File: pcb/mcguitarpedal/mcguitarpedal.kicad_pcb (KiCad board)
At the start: 2 copper layers, 123 x 113.5 mm, 123 parts, among them J1 OUT, J10 ENC2, J11 ENC3, J12 BTN_MTX, J2 EXP, J3 IN, J4 PWR, J5 PWR_IN, J6 PREAMP_HEADERS, J7 ILI9488 Module, J8 POT_HP_VOLUME_10k, J9 ENC1, Q1 2N3904, Q2 BC416, SW1 SW_PWR, SW2 SW_BYPASS, SW3 SW_TUNER, SW4 SW_PRESET, SW5 LINE_LEVEL, U1 Teensy4.1, U2 Teensy Audio Board, U3 LM4562, U4 STPDWN-3P-5V, U5 AMS1117-3.3, U6 74HCT595, U7 74HC148

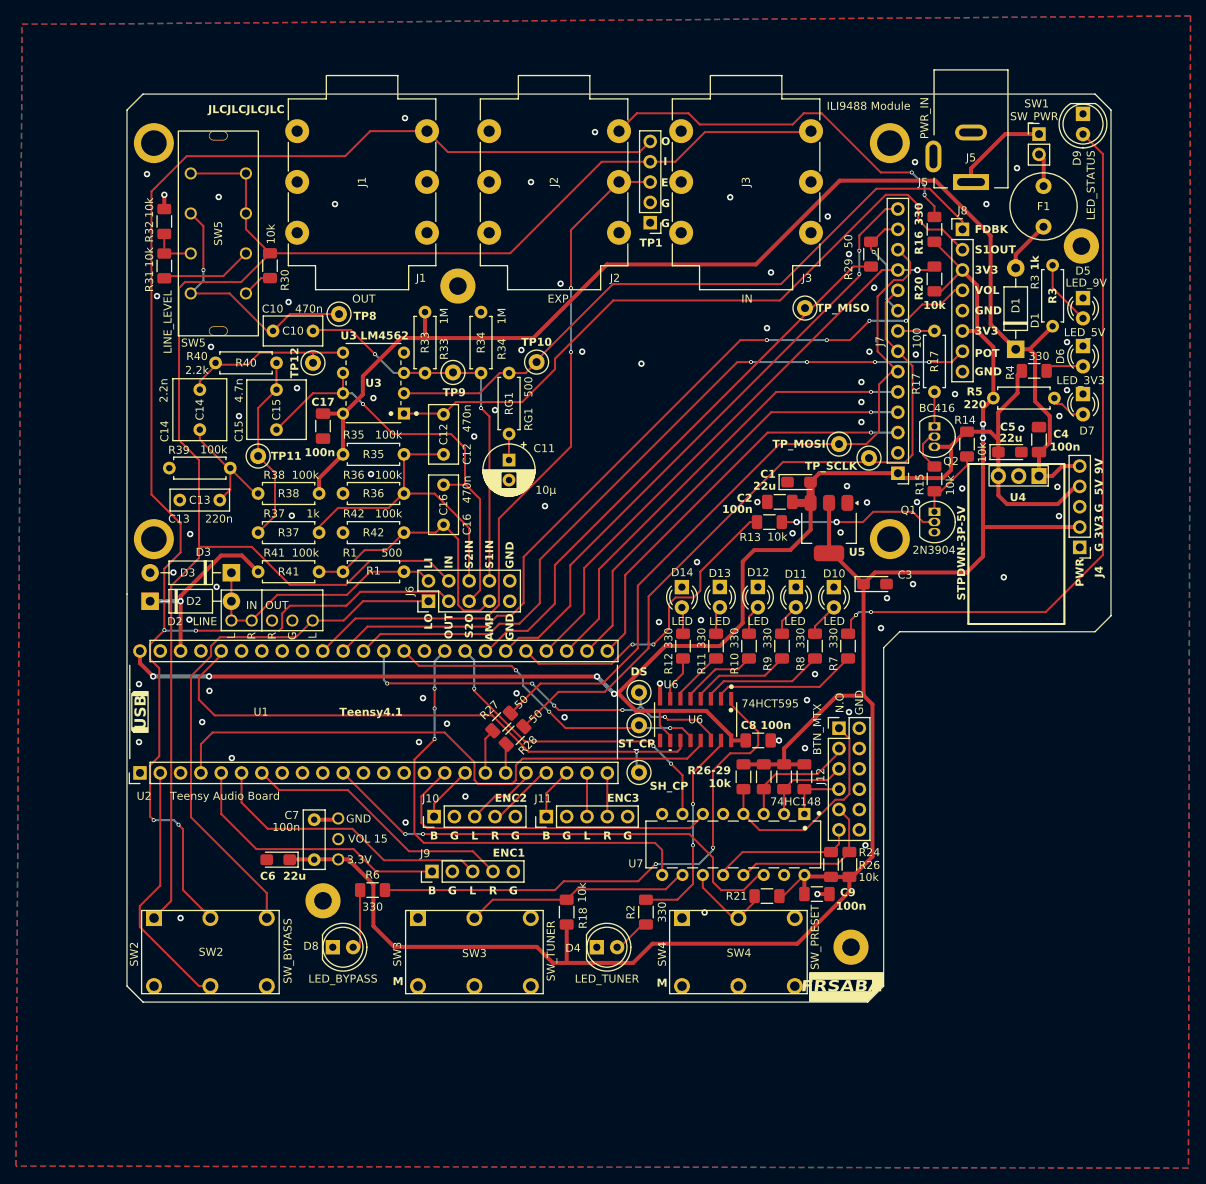
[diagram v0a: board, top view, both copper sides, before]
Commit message: Missing models, PCB pdf exports
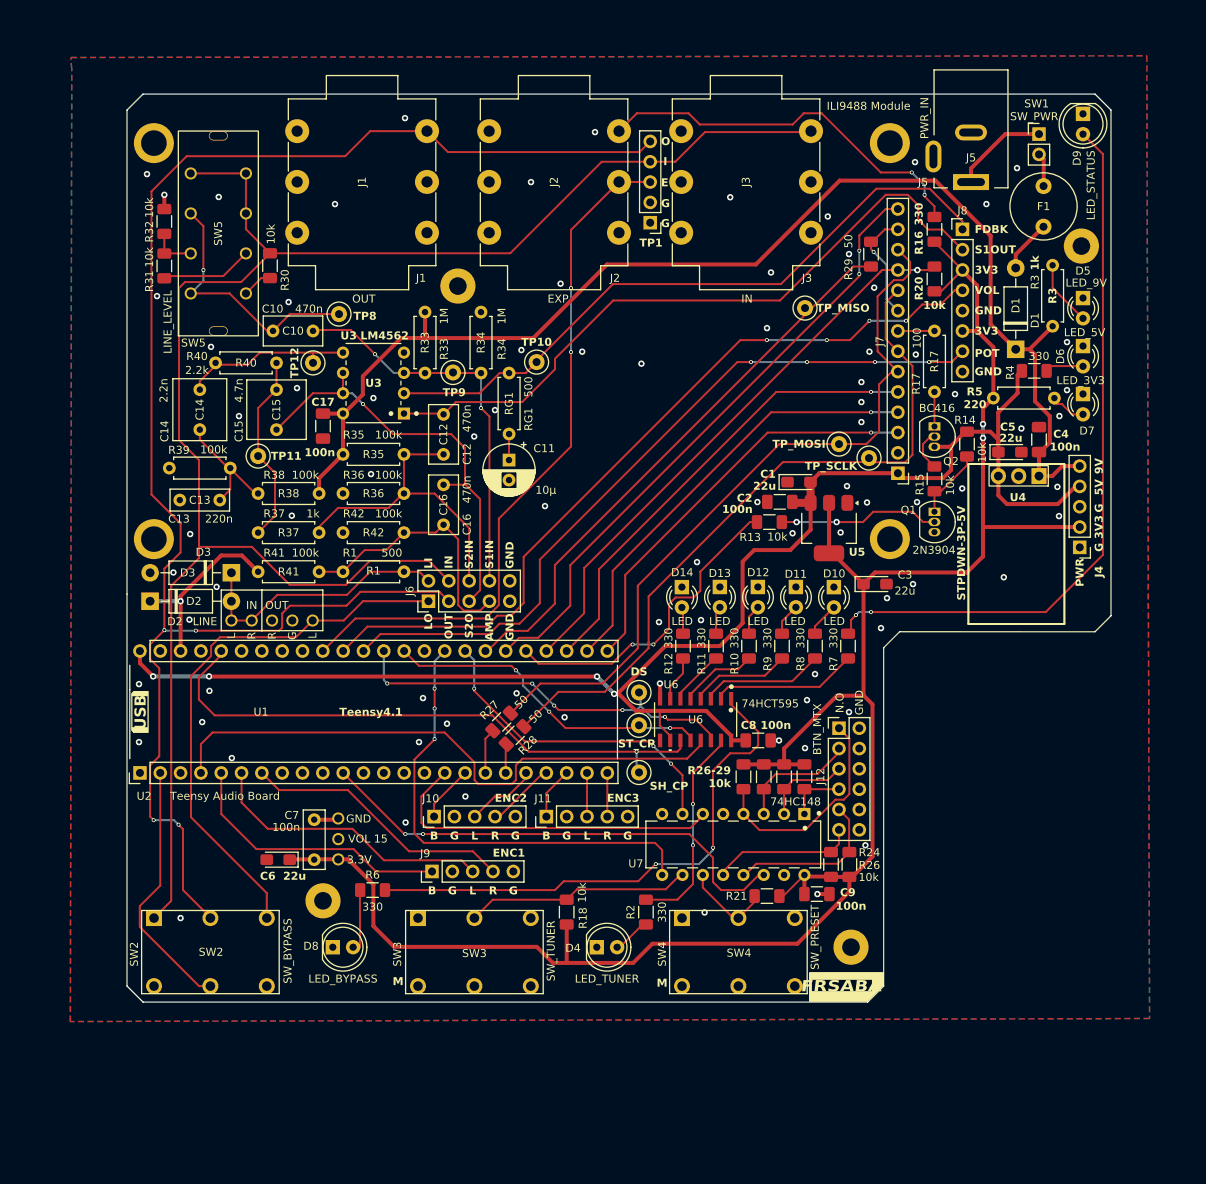
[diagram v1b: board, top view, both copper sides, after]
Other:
- board text removed: "JLCJLCJLCJLC"
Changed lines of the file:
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@@
 	)
 	(property "R_BIAS" "100k")
-	(property "R_BIAS_IN" "1M")
+	(property "R_BIAS_IN" "100k")
 	(net 0 "")
 	(net 1 "Net-(SW5-D)")
@@
 		)
 		(fp_text user "${REFERENCE}"
-			(at 0 0 360)
+			(at 0 0 0)
 			(layer "F.Fab")
 			(effects
@@
 		(property "Value" "22u"
 			(at 3.75 0.85 0)
-			(layer "F.Fab")
+			(layer "F.SilkS")
 			(effects
 				(font
@@
 			(pintype "power_in")
 		)
+		(model "${KICAD_MCGUITARPEDAL_MODELS}/P0008A.stp"
+			(offset
+				(xyz 3.78 -3.8 0)
+			)
+			(scale
+				(xyz 1 1 1)
+			)
+			(rotate
+				(xyz 0 0 0)
+			)
+		)
 	)
 	(footprint "mcguitarpedal:SW_PUSH_DPDT"
@@
 			(pintype "passive+no_connect")
 		)
-		(model "${KICAD8_3DMODEL_DIR}/Connector_BarrelJack.3dshapes/BarrelJack_Kycon_KLDX-0202-xC_Horizontal.wrl"
+		(model "${KIPRJMOD}/lib/3D_models/DC_Power_Jack_PCB_Mounted_2.1mm.step"
 			(offset
 				(xyz 0 0 0)
@@
 		(tags "resistor handsolder")
 		(property "Reference" "R16"
-			(at 1.691201 1.932 270)
+			(at 1.691201 1.932 -90)
 			(layer "F.SilkS")
 			(effects
@@
 		)
 		(property "Value" "330"
-			(at -1.908799 1.932 270)
+			(at -1.908799 1.932 -90)
 			(layer "F.SilkS")
 			(effects
@@
 			(pintype "power_in")
 		)
+		(model "${KIPRJMOD}/lib/74HCT595/SOIC-16_ONS.step"
+			(offset
+				(xyz 0 0 0)
+			)
+			(scale
+				(xyz 1 1 1)
+			)
+			(rotate
+				(xyz 0 0 0)
+			)
+		)
 	)
 	(footprint "mcguitarpedal:LED_D3.0mm"
@@
 		(tags "74HC148 ")
 		(property "Reference" "U7"
-			(at 6.211 21.076 180)
+			(at 6.211 21.076 360)
 			(layer "F.SilkS")
 			(effects
@@
 			(pintype "power_in")
 		)
+		(model "${KICAD_MCGUITARPEDAL_MODELS}/N16_TEX.step"
+			(offset
+				(xyz 0 0 0)
+			)
+			(scale
+				(xyz 1 1 1)
+			)
+			(rotate
+				(xyz 0 0 0)
+			)
+		)
 	)
 	(footprint "mcguitarpedal:Floating Encoder"
@@
 		)
 	)
-	(gr_text "JLCJLCJLCJLC"
-		(at 73.2 27.5 0)
-		(layer "F.SilkS")
-		(effects
-			(font
-				(size 1 1)
-				(thickness 0.2)
-				(bold yes)
-			)
-			(justify right bottom)
-		)
-	)
 	(gr_text "N.O"
 		(at 142.6 101.1 90)
@@
 	)
 	(zone
-		(net 43)
-		(net_name "Net-(J7-SCK)")
+		(net 42)
+		(net_name "Net-(J7-SDI(MOSI))")
 		(layer "F.Cu")
 		(name "$teardrop_padvia$")
 		(hatch full 0.1)
-		(priority 30002)
+		(priority 30001)
 		(attr
 			(teardrop
@@
 		(polygon
 			(pts
-				(xy 144.004509 71.125) (xy 144.278528 71.117413) (xy 144.530743 71.099433) (xy 144.759995 71.078226)
-				(xy 144.965124 71.06096) (xy 145.144971 71.054803) (xy 145.298374 71.066922) (xy 145.424175 71.104486)
-				(xy 145.521214 71.174662) (xy 146.251 70.5) (xy 145.31024 70.197149) (xy 145.256893 70.311335) (xy 145.169383 70.42805)
-				(xy 145.049097 70.541819) (xy 144.897419 70.647173) (xy 144.715736 70.73864) (xy 144.505433 70.810748)
-				(xy 144.267895 70.858025) (xy 144.004509 70.875)
+				(xy 144.9 68.625) (xy 144.610673 68.620769) (xy 144.343891 68.607147) (xy 144.101954 68.582738)
+				(xy 143.887163 68.546144) (xy 143.70182 68.49597) (xy 143.548227 68.430818) (xy 143.428683 68.349294)
+				(xy 143.345491 68.25) (xy 142.499 68.75) (xy 143.345491 69.25) (xy 143.428683 69.150705) (xy 143.548227 69.06918)
+				(xy 143.70182 69.004029) (xy 143.887163 68.953855) (xy 144.101954 68.917261) (xy 144.343891 68.892851)
+				(xy 144.610673 68.87923) (xy 144.9 68.875)
 			)
 		)
@@
 		(name "$teardrop_padvia$")
 		(hatch full 0.1)
-		(priority 30005)
+		(priority 30004)
 		(attr
 			(teardrop
@@
 		(polygon
 			(pts
-				(xy 140.127604 50.55122) (xy 139.933634 50.717404) (xy 139.734444 50.839839) (xy 139.535594 50.922862)
-				(xy 139.342646 50.970808) (xy 139.161163 50.988016) (xy 138.996706 50.978821) (xy 138.854835 50.947561)
-				(xy 138.741115 50.898572) (xy 138.249293 51.750707) (xy 139.247842 51.760847) (xy 139.2728 51.647186)
-				(xy 139.340914 51.539641) (xy 139.445909 51.432947) (xy 139.581505 51.321841) (xy 139.741428 51.201056)
-				(xy 139.919399 51.06533) (xy 140.109142 50.909398) (xy 140.30438 50.727996)
+				(xy 137.227996 53.80438) (xy 137.409398 53.609142) (xy 137.56533 53.419399) (xy 137.701056 53.241428)
+				(xy 137.821841 53.081505) (xy 137.932947 52.945909) (xy 138.039641 52.840914) (xy 138.147186 52.7728)
+				(xy 138.260847 52.747842) (xy 138.250707 51.749293) (xy 137.398572 52.241115) (xy 137.447561 52.354835)
+				(xy 137.478821 52.496706) (xy 137.488016 52.661163) (xy 137.470808 52.842646) (xy 137.422862 53.035594)
+				(xy 137.339839 53.234444) (xy 137.217404 53.433634) (xy 137.05122 53.627604)
 			)
 		)
@@
 	)
 	(zone
-		(net 12)
-		(net_name "/39_TFT_MISO")
+		(net 43)
+		(net_name "Net-(J7-SCK)")
 		(layer "F.Cu")
 		(name "$teardrop_padvia$")
 		(hatch full 0.1)
-		(priority 30004)
+		(priority 30002)
 		(attr
 			(teardrop
@@
 		(polygon
 			(pts
-				(xy 137.227996 53.80438) (xy 137.409398 53.609142) (xy 137.56533 53.419399) (xy 137.701056 53.241428)
-				(xy 137.821841 53.081505) (xy 137.932947 52.945909) (xy 138.039641 52.840914) (xy 138.147186 52.7728)
-				(xy 138.260847 52.747842) (xy 138.250707 51.749293) (xy 137.398572 52.241115) (xy 137.447561 52.354835)
-				(xy 137.478821 52.496706) (xy 137.488016 52.661163) (xy 137.470808 52.842646) (xy 137.422862 53.035594)
-				(xy 137.339839 53.234444) (xy 137.217404 53.433634) (xy 137.05122 53.627604)
+				(xy 144.004509 71.125) (xy 144.278528 71.117413) (xy 144.530743 71.099433) (xy 144.759995 71.078226)
+				(xy 144.965124 71.06096) (xy 145.144971 71.054803) (xy 145.298374 71.066922) (xy 145.424175 71.104486)
+				(xy 145.521214 71.174662) (xy 146.251 70.5) (xy 145.31024 70.197149) (xy 145.256893 70.311335) (xy 145.169383 70.42805)
+				(xy 145.049097 70.541819) (xy 144.897419 70.647173) (xy 144.715736 70.73864) (xy 144.505433 70.810748)
+				(xy 144.267895 70.858025) (xy 144.004509 70.875)
 			)
 		)
 	)
 	(zone
-		(net 42)
-		(net_name "Net-(J7-SDI(MOSI))")
+		(net 12)
+		(net_name "/39_TFT_MISO")
 		(layer "F.Cu")
 		(name "$teardrop_padvia$")
 		(hatch full 0.1)
-		(priority 30001)
+		(priority 30005)
 		(attr
 			(teardrop
@@
 		(polygon
 			(pts
-				(xy 144.9 68.625) (xy 144.610673 68.620769) (xy 144.343891 68.607147) (xy 144.101954 68.582738)
-				(xy 143.887163 68.546144) (xy 143.70182 68.49597) (xy 143.548227 68.430818) (xy 143.428683 68.349294)
-				(xy 143.345491 68.25) (xy 142.499 68.75) (xy 143.345491 69.25) (xy 143.428683 69.150705) (xy 143.548227 69.06918)
-				(xy 143.70182 69.004029) (xy 143.887163 68.953855) (xy 144.101954 68.917261) (xy 144.343891 68.892851)
-				(xy 144.610673 68.87923) (xy 144.9 68.875)
+				(xy 140.127604 50.55122) (xy 139.933634 50.717404) (xy 139.734444 50.839839) (xy 139.535594 50.922862)
+				(xy 139.342646 50.970808) (xy 139.161163 50.988016) (xy 138.996706 50.978821) (xy 138.854835 50.947561)
+				(xy 138.741115 50.898572) (xy 138.249293 51.750707) (xy 139.247842 51.760847) (xy 139.2728 51.647186)
+				(xy 139.340914 51.539641) (xy 139.445909 51.432947) (xy 139.581505 51.321841) (xy 139.741428 51.201056)
+				(xy 139.919399 51.06533) (xy 140.109142 50.909398) (xy 140.30438 50.727996)
 			)
 		)
@@
 		(polygon
 			(pts
-				(xy 46.482 16.256) (xy 186.436 15.24) (xy 186.182 159.258) (xy 39.624 159.004) (xy 40.386 16.256)
+				(xy 46.480543 20.428919) (xy 180.974543 20.212919) (xy 181.320543 140.550919) (xy 46.422543 140.936919)
+				(xy 46.584543 21.868919)
 			)
 		)
@@
 			)
 		)
+	)
+	(zone
+		(net 0)
+		(net_name "")
+		(layer "Eco2.User")
+		(hatch edge 0.5)
+		(connect_pads
+			(clearance 0.5)
+		)
+		(min_thickness 0.25)
+		(filled_areas_thickness no)
+		(fill yes
+			(thermal_gap 0.5)
+			(thermal_bridge_width 0.5)
+		)
+		(polygon
+			(pts
+				(xy 177.8 22.86) (xy 48.26 20.32) (xy 45.72 142.24) (xy 180.34 142.24)
+			)
+		)
